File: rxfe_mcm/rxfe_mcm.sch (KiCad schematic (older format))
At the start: 0 parts

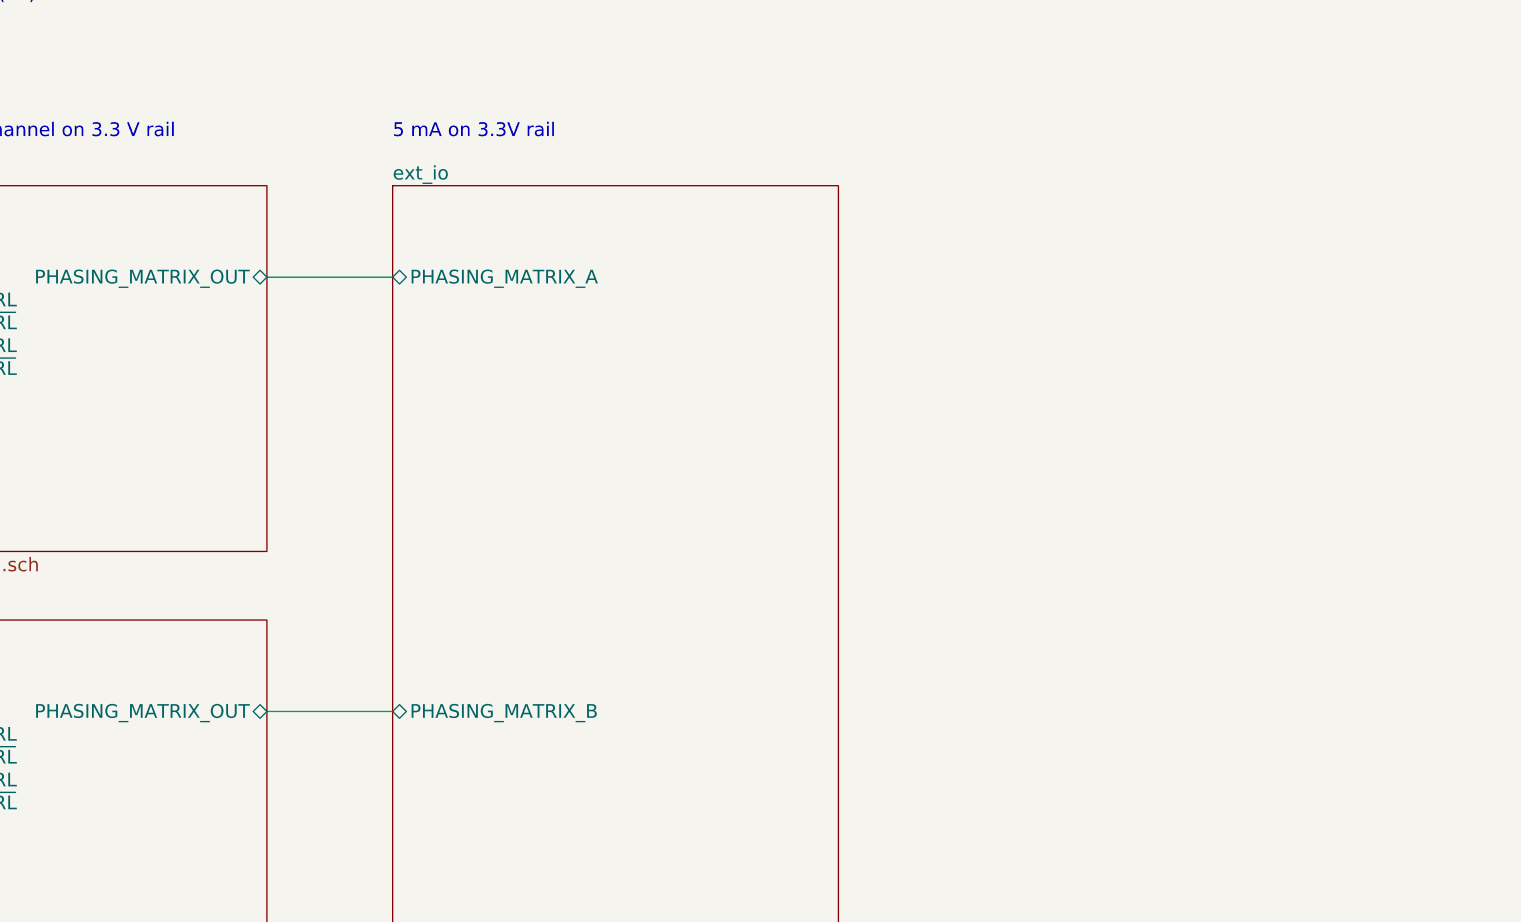
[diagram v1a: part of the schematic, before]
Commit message: added tvs diodes to external connections on mcm_rxfe
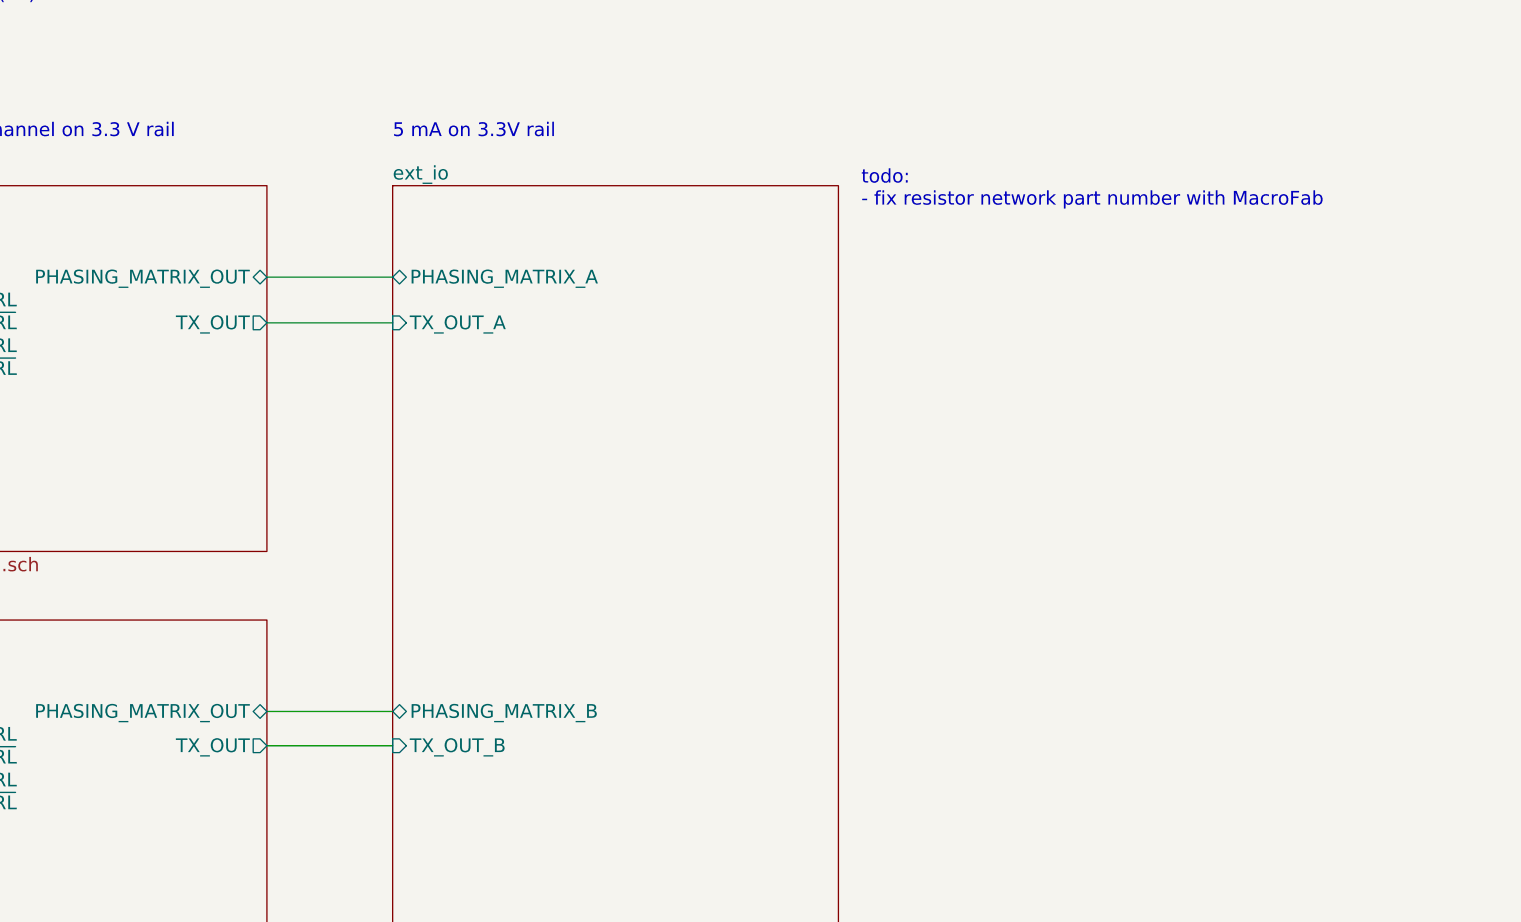
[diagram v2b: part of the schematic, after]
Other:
- note added: "todo:\n- fix resistor network part number with MacroFab"
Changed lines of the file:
@@
 LIBS:74hc04_full
 LIBS:hmc595
-LIBS:hmc475
 LIBS:smp1330-005lf
 LIBS:hmc542blp4e
@@
 F6 "AUX_IO_A" I L 6650 5600 60
 F7 "AUX_IO_B" I L 6650 5700 60
+F8 "TX_OUT_A" I L 6650 2250 60
+F9 "TX_OUT_B" I L 6650 4100 60
 $EndSheet
 Text Notes 2400 1450 0    60   ~ 0
@@
 F12 "~AMP1_CTRL" I L 4450 2250 60
 F13 "~AMP2_CTRL" I L 4450 2450 60
+F14 "TX_OUT" O R 6100 2250 60
 $EndSheet
 Wire Wire Line
@@
 F12 "~AMP1_CTRL" I L 4450 4150 60
 F13 "~AMP2_CTRL" I L 4450 4350 60
+F14 "TX_OUT" O R 6100 4100 60
 $EndSheet
 Wire Wire Line
@@
 Text Notes 1300 950  0    60   ~ 0
 fits in V1145-ND snap-in rack\nor, break off tabs for bud EXT-9166 case
+Text Notes 8700 1750 0    60   ~ 0
+todo:\n- fix resistor network part number with MacroFab
+Wire Wire Line
+	6100 2250 6650 2250
+Wire Wire Line
+	6100 4100 6650 4100
 $EndSCHEMATC

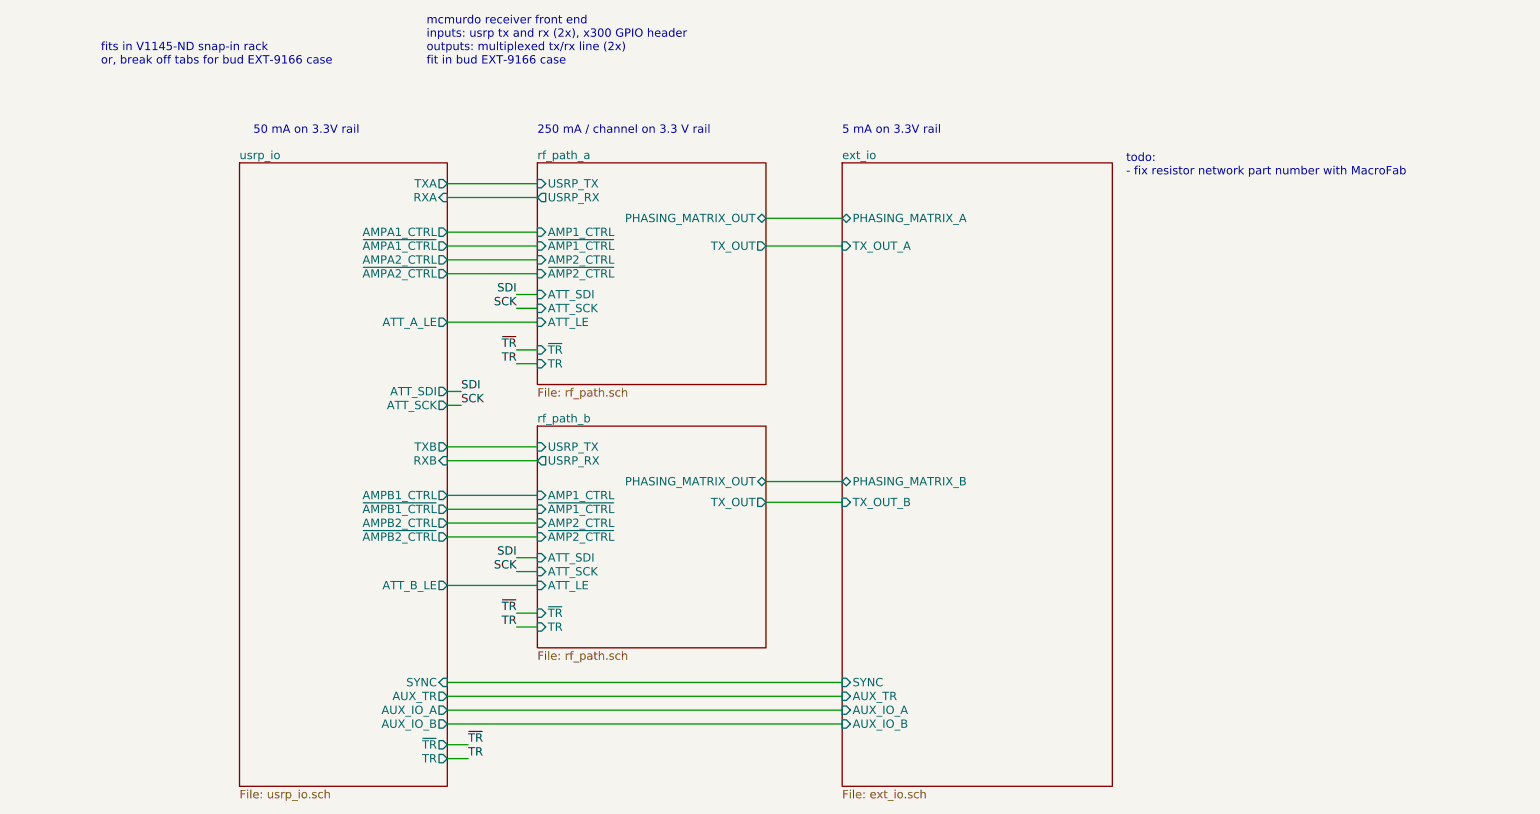
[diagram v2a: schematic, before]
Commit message: add input protection to mcm usrp front end, modified to also work at kodiak
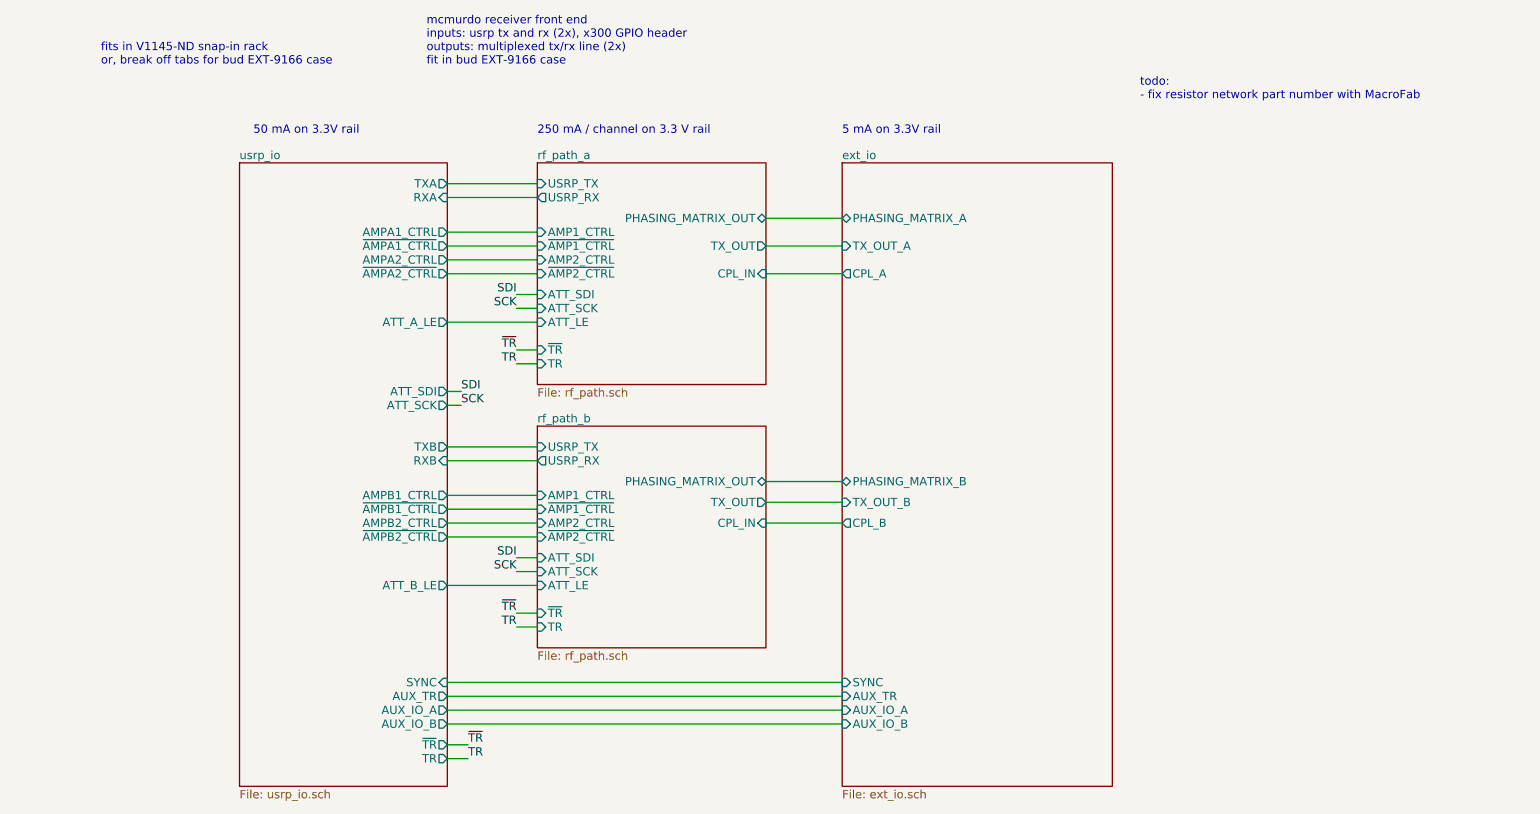
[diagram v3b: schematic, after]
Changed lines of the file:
@@
 F8 "TX_OUT_A" I L 6650 2250 60
 F9 "TX_OUT_B" I L 6650 4100 60
+F10 "CPL_A" O L 6650 2450 59
+F11 "CPL_B" O L 6650 4250 59
 $EndSheet
 Text Notes 2400 1450 0    60   ~ 0
@@
 F13 "~AMP2_CTRL" I L 4450 2450 60
 F14 "TX_OUT" O R 6100 2250 60
+F15 "CPL_IN" I R 6100 2450 59
 $EndSheet
 Wire Wire Line
@@
 F13 "~AMP2_CTRL" I L 4450 4350 60
 F14 "TX_OUT" O R 6100 4100 60
+F15 "CPL_IN" I R 6100 4250 59
 $EndSheet
 Wire Wire Line
@@
 Text Notes 1300 950  0    60   ~ 0
 fits in V1145-ND snap-in rack\nor, break off tabs for bud EXT-9166 case
-Text Notes 8700 1750 0    60   ~ 0
+Text Notes 8800 1200 0    60   ~ 0
 todo:\n- fix resistor network part number with MacroFab
 Wire Wire Line
@@
 Wire Wire Line
 	6100 4100 6650 4100
+Wire Wire Line
+	6100 2450 6650 2450
+Wire Wire Line
+	6100 4250 6650 4250
 $EndSCHEMATC

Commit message: added input/output protection to kodiak control board, switched all connectors to through hole
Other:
- note added: "todo:\n- add buffered differential TR output"
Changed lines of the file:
@@
 EESchema Schematic File Version 2
-LIBS:rxfe_mcm-rescue
 LIBS:power
 LIBS:device
@@
 LIBS:74hc04_full
 LIBS:hmc595
-LIBS:hmc475
 LIBS:smp1330-005lf
 LIBS:hmc542blp4e
@@
 Wire Wire Line
 	6100 4250 6650 4250
+Text Notes 8800 1400 0    60   ~ 0
+todo:\n- add buffered differential TR output
 $EndSCHEMATC

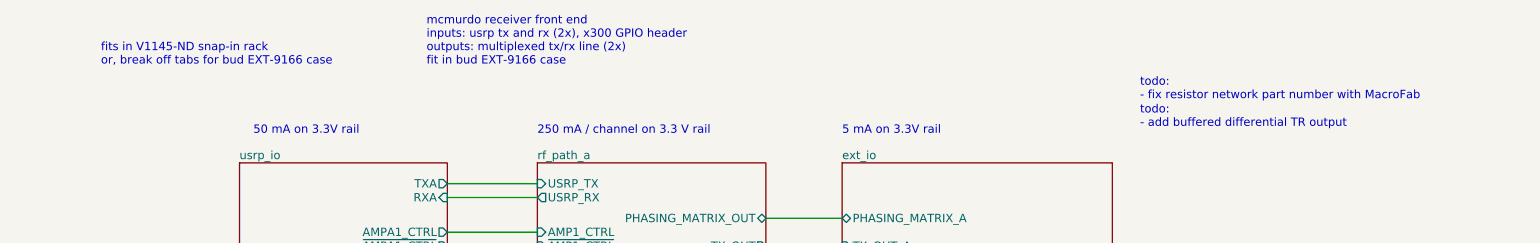
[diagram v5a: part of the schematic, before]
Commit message: removed tx path amp, erc fixes
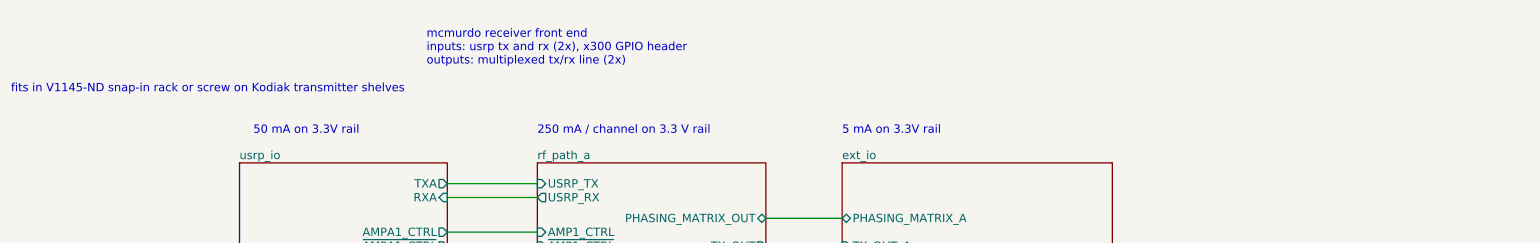
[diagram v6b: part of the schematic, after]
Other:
- note added: "fits in V1145-ND snap-in rack or screw on Kodiak transmitter shelves"
- note added: "mcmurdo receiver front end\ninputs: usrp tx and rx (2x), x300 GPIO header\noutputs: multiplexed tx/rx line (2x)"
- note removed: "fits in V1145-ND snap-in rack\nor, break off tabs for bud EXT-9166 case"
- note removed: "mcmurdo receiver front end\ninputs: usrp tx and rx (2x), x300 GPIO header\noutputs: multiplexed tx/rx line (2x)\nfit in bud EXT-9166 case"
- note removed: "todo:\n- add buffered differential TR output"
- note removed: "todo:\n- fix resistor network part number with MacroFab"
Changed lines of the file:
@@
 LIBS:adp7158
 LIBS:pe4312
+LIBS:isl3295efhz-t
 LIBS:rxfe_mcm-cache
 EELAYER 25 0
@@
 $EndDescr
 Text Notes 3650 950  0    60   ~ 0
-mcmurdo receiver front end\ninputs: usrp tx and rx (2x), x300 GPIO header\noutputs: multiplexed tx/rx line (2x)\nfit in bud EXT-9166 case
+mcmurdo receiver front end\ninputs: usrp tx and rx (2x), x300 GPIO header\noutputs: multiplexed tx/rx line (2x)
 $Sheet
 S 2300 1650 1500 4500
@@
 Text Notes 6650 1450 0    60   ~ 0
 5 mA on 3.3V rail
-Text Notes 1300 950  0    60   ~ 0
-fits in V1145-ND snap-in rack\nor, break off tabs for bud EXT-9166 case
-Text Notes 8800 1200 0    60   ~ 0
-todo:\n- fix resistor network part number with MacroFab
+Text Notes 650  1150 0    60   ~ 0
+fits in V1145-ND snap-in rack or screw on Kodiak transmitter shelves
 Wire Wire Line
 	6100 2250 6650 2250
@@
 Wire Wire Line
 	6100 4250 6650 4250
-Text Notes 8800 1400 0    60   ~ 0
-todo:\n- add buffered differential TR output
 $EndSCHEMATC
